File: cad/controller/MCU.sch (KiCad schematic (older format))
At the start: 19 parts

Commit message: Added decoupling inductors and capacitors
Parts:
- removed C?: C, symbol Device:C
- removed L?: L_Core_Ferrite, symbol Device:L_Core_Ferrite
- added C? (x2): 10uF, Capacitor_SMD:C_0603_1608Metric, symbol Device:C
- added C? (x3): 100nF, Capacitor_SMD:C_0603_1608Metric, symbol Device:C
- added FB?: BLM21, Inductor_SMD:L_0805_2012Metric, symbol Device:Ferrite_Bead
- added J?: Conn_01x04, symbol Connector_Generic:Conn_01x04
- added U?: TXB0104D, Package_SO:SOIC-14_3.9x8.7mm_P1.27mm, symbol Logic_LevelTranslator:TXB0104D
- C? (x3): value C -> 100nF; footprint (none) -> Capacitor_SMD:C_0603_1608Metric
- C? (x2): footprint (none) -> Capacitor_SMD:C_0603_1608Metric
- R? (x5): footprint (none) -> Resistor_SMD:R_0603_1608Metric
- Y?: value Crystal -> 18MHz
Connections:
- net labels added: CS, MISO, MOSI, SCLK
- net labels removed: ANA-
- wire segments 103 -> 132
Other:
- note added: "18 MHz\nECS-180-S-5PX-TR"
- note added: "TODO\n- Atmega328 pin mapping\n- Route ADC input 1"
- moved on the sheet: C?

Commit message: Ordered components
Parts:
- gave numbers to parts that had none: 25

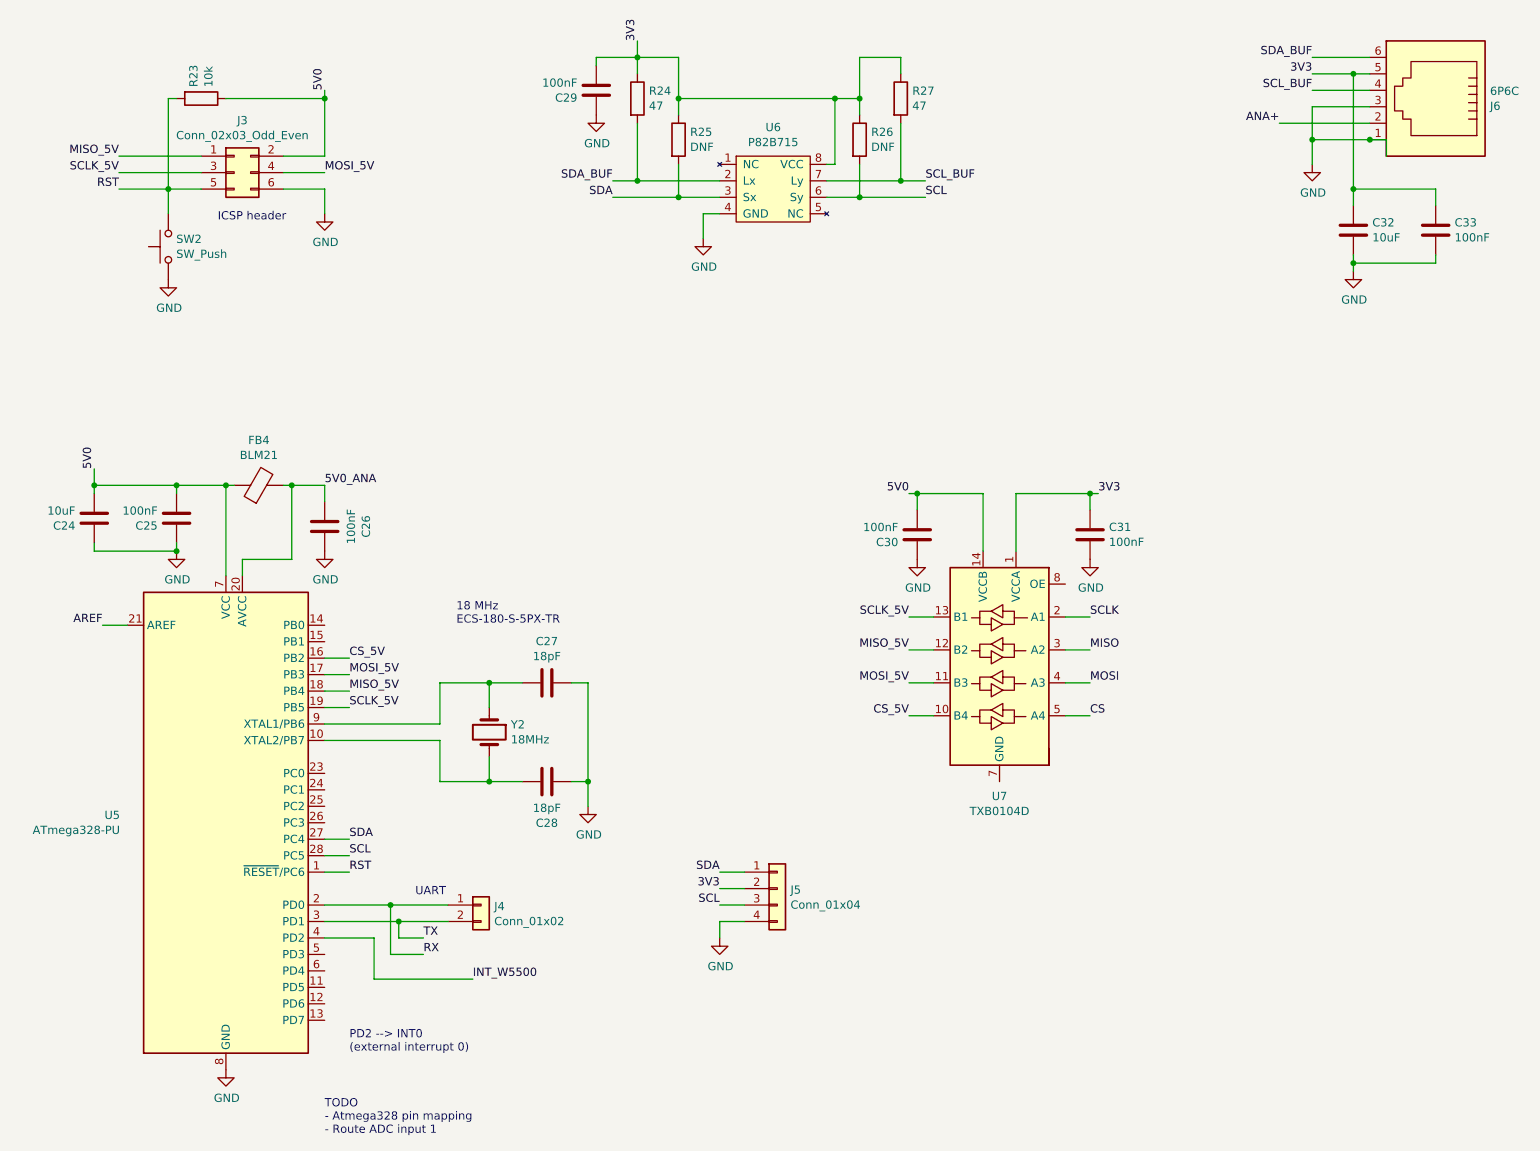
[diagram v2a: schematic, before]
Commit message: Changed I2C buffer to PCA1517, added termination network on RJ11 I2C lines
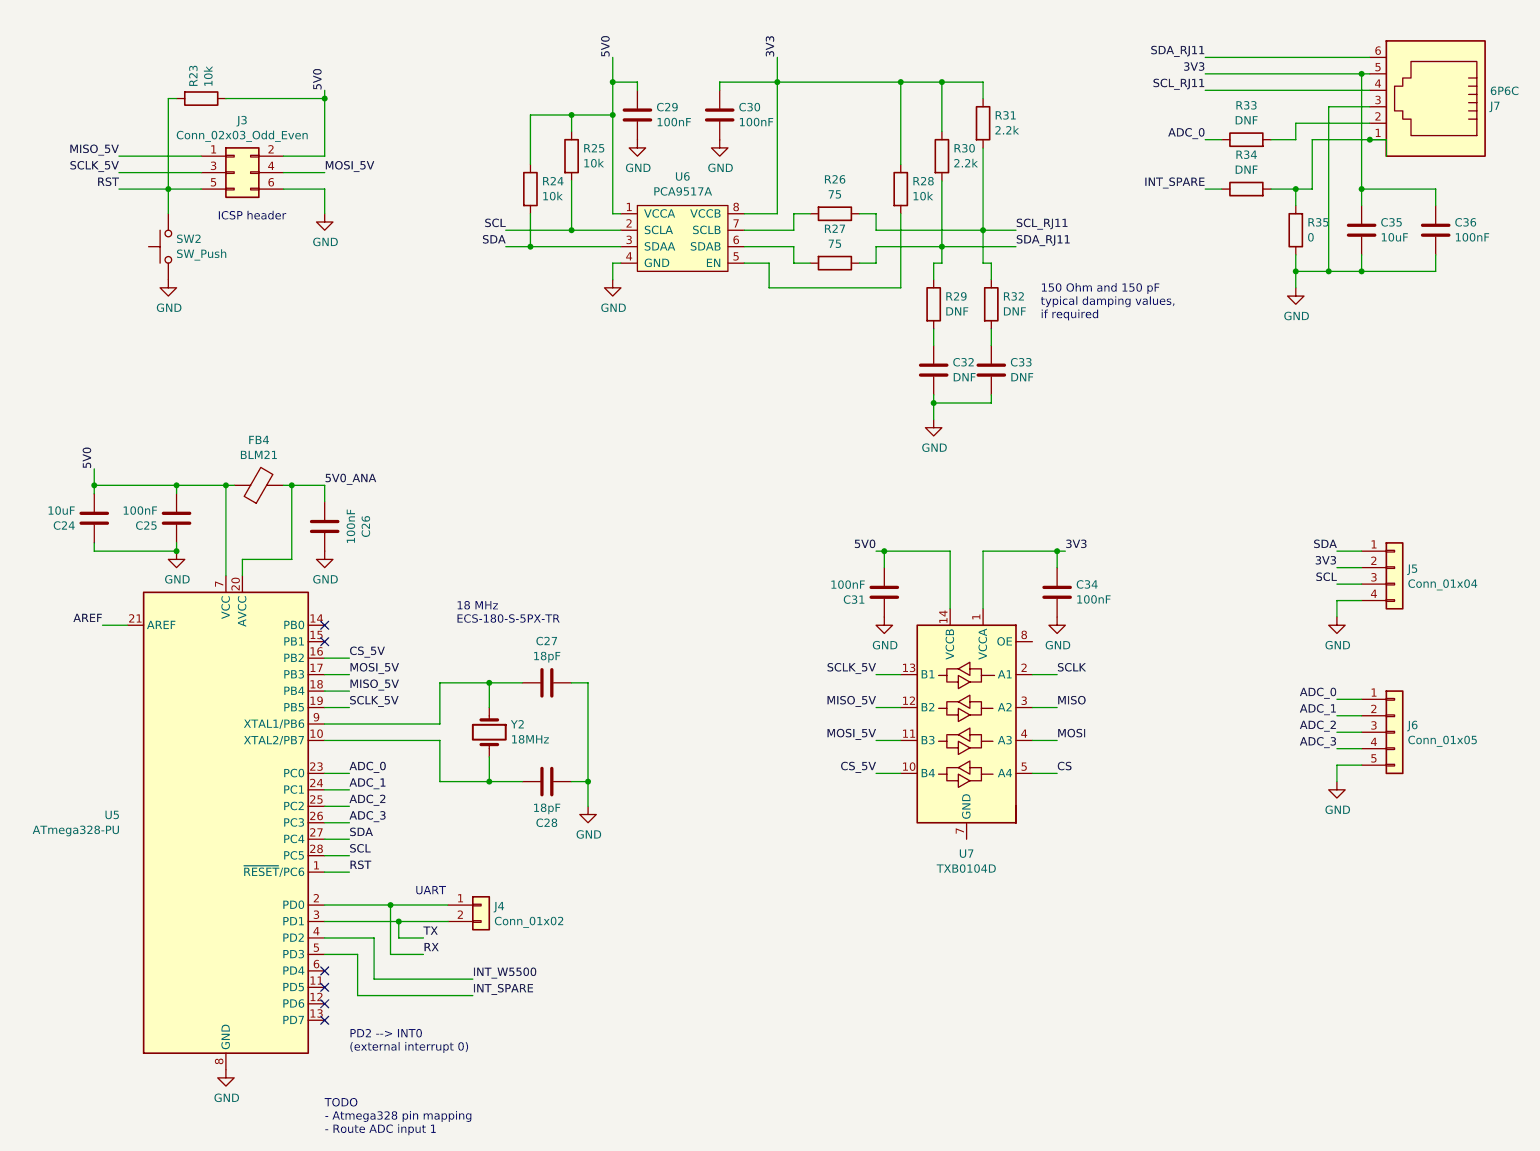
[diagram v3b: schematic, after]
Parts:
- removed U6: P82B715, symbol custom:P82B715
- added C30: 100nF, Capacitor_SMD:C_0603_1608Metric, symbol Device:C
- added C32, C33: DNF, Capacitor_SMD:C_0603_1608Metric, symbol Device:C
- added J6: Conn_01x05, symbol Connector_Generic:Conn_01x05
- added R28: 10k, Resistor_SMD:R_0603_1608Metric, symbol Device:R
- added R29, R32, R33, R34: DNF, Resistor_SMD:R_0603_1608Metric, symbol Device:R
- added R30, R31: 2.2k, Resistor_SMD:R_0603_1608Metric, symbol Device:R
- added R35: 0, Resistor_SMD:R_0603_1608Metric, symbol Device:R
- added U6: PCA9517A, symbol custom:PCA9517A
- R24: value 47 -> 10k
- R25: value DNF -> 10k
- R26: value DNF -> 75
- R27: value 47 -> 75
- renumbered C30 to C31, C31 to C34, C32 to C35, C33 to C36, J6 to J7
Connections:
- net 3V3: now also C30.1, R28.1, R30.1, R31.1, U6.8 (VCCB); no longer C29.2, R24.1, R25.1, R26.1, R27.1
- net 5V0: now also C29.1, R24.1, R25.1, U6.1 (VCCA)
- net GND: now also C29.2, C30.2, C32.2, C33.2, J6.5 (Pin_5), R35.1, U6.4 (GND); no longer C29.1, J7.1
- net SCL: now also R25.2, U6.2 (SCLA); no longer R26.2
- net SDA: now also R24.2, U6.3 (SDAA); no longer R25.2
- net ADC_0: now reaches U5.23 (PC0)
- net ADC_0: now also J6.1 (Pin_1), R33.1
- net ADC_1: now reaches U5.24 (PC1)
- net ADC_1: now also J6.2 (Pin_2)
- net ADC_2: now reaches U5.25 (PC2)
- net ADC_2: now also J6.3 (Pin_3)
- net ADC_3: now reaches U5.26 (PC3)
- net ADC_3: now also J6.4 (Pin_4)
- net INT_SPARE: now reaches U5.5 (PD3)
- net INT_SPARE: now also R34.1
- net ANA+: no longer names the net of J7.2
- net ANA+: now also R33.2
- net SCL_BUF: no longer names the net of R27.2
- net SCL_BUF: now also U6.6 (SDAB); no longer J7.4
- net SDA_BUF renamed SDA_RJ11
- net SDA_RJ11: now also R27.1, R29.1, R30.2; no longer R24.2
- new net: J7.1, R34.2, R35.2
- new net: R28.2, U6.5 (EN)
- new net: R26.2, U6.7 (SCLB)
- new net: C32.1, R29.2
- new net: C33.1, R32.2
- new net SCL_RJ11: J7.4, R26.1, R31.2, R32.1
- no-connect marks 0 -> 6
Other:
- note added: "150 Ohm and 150 pF\ntypical damping values,\nif required"
- moved on the sheet: C31, C34, C35, J5, U7

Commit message: Added custom libraries submodule and updated the symbol tables in the kicad projects
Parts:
- U6: symbol custom:PCA9517A -> custom_digital:PCA9517A
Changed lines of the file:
@@
 INT_SPARE
 $Comp
-L custom:PCA9517A U6
+L custom_digital:PCA9517A U6
 U 1 1 624DB520
 P 4950 1700

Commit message: Started associating footprints with controller schematic
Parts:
- J3: footprint (none) -> Connector_PinHeader_2.54mm:PinHeader_2x03_P2.54mm_Vertical
- J4: footprint (none) -> Connector_PinSocket_2.54mm:PinSocket_1x02_P2.54mm_Vertical
- J5: footprint (none) -> Connector_Molex:Molex_KK-254_AE-6410-04A_1x04_P2.54mm_Vertical
- J6: footprint (none) -> Connector_PinHeader_2.54mm:PinHeader_1x05_P2.54mm_Vertical
- SW2: footprint (none) -> Button_Switch_THT:SW_PUSH_6mm
- U6: footprint (none) -> Package_SO:TSSOP-8_3x3mm_P0.65mm
- Y2: footprint (none) -> Crystal:Crystal_SMD_HC49-SD_HandSoldering
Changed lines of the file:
@@
 F 0 "Y2" V 3704 5131 50  0000 L CNN
 F 1 "18MHz" V 3795 5131 50  0000 L CNN
-F 2 "" H 3750 5000 50  0001 C CNN
+F 2 "Crystal:Crystal_SMD_HC49-SD_HandSoldering" H 3750 5000 50  0001 C CNN
 F 3 "~" H 3750 5000 50  0001 C CNN
 	1    3750 5000
@@
 F 0 "J3" H 2250 1917 50  0000 C CNN
 F 1 "Conn_02x03_Odd_Even" H 2250 1826 50  0000 C CNN
-F 2 "" H 2200 1600 50  0001 C CNN
+F 2 "Connector_PinHeader_2.54mm:PinHeader_2x03_P2.54mm_Vertical" H 2200 1600 50  0001 C CNN
 F 3 "~" H 2200 1600 50  0001 C CNN
 	1    2200 1600
@@
 F 0 "SW2" V 1846 2002 50  0000 R CNN
 F 1 "SW_Push" V 1755 2002 50  0000 R CNN
-F 2 "" H 1800 2250 50  0001 C CNN
+F 2 "Button_Switch_THT:SW_PUSH_6mm" H 1800 2250 50  0001 C CNN
 F 3 "~" H 1800 2250 50  0001 C CNN
 	1    1800 2050
@@
 F 0 "J4" H 3780 6042 50  0000 L CNN
 F 1 "Conn_01x02" H 3780 5951 50  0000 L CNN
-F 2 "" H 3700 6050 50  0001 C CNN
+F 2 "Connector_PinSocket_2.54mm:PinSocket_1x02_P2.54mm_Vertical" H 3700 6050 50  0001 C CNN
 F 3 "~" H 3700 6050 50  0001 C CNN
 	1    3700 6050
@@
 F 0 "J5" H 9330 3992 50  0000 L CNN
 F 1 "Conn_01x04" H 9330 3901 50  0000 L CNN
-F 2 "" H 9250 4000 50  0001 C CNN
+F 2 "Connector_Molex:Molex_KK-254_AE-6410-04A_1x04_P2.54mm_Vertical" H 9250 4000 50  0001 C CNN
 F 3 "~" H 9250 4000 50  0001 C CNN
 	1    9250 4000
@@
 F 0 "J6" H 9330 5042 50  0000 L CNN
 F 1 "Conn_01x05" H 9330 4951 50  0000 L CNN
-F 2 "" H 9250 5000 50  0001 C CNN
+F 2 "Connector_PinHeader_2.54mm:PinHeader_1x05_P2.54mm_Vertical" H 9250 5000 50  0001 C CNN
 F 3 "~" H 9250 5000 50  0001 C CNN
 	1    9250 5000
@@
 F 0 "U6" H 4925 1775 50  0000 C CNN
 F 1 "PCA9517A" H 4925 1684 50  0000 C CNN
-F 2 "" H 4950 1700 50  0001 C CNN
+F 2 "Package_SO:TSSOP-8_3x3mm_P0.65mm" H 4950 1700 50  0001 C CNN
 F 3 "" H 4950 1700 50  0001 C CNN
 	1    4950 1700

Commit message: Ready to begin layout
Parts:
- J7: footprint (none) -> custom:E5566-Q0LK22-L
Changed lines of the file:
@@
 F 0 "J7" H 9170 1204 50  0000 R CNN
 F 1 "6P6C" H 9170 1295 50  0000 R CNN
-F 2 "" V 9500 1225 50  0001 C CNN
+F 2 "custom:E5566-Q0LK22-L" V 9500 1225 50  0001 C CNN
 F 3 "~" V 9500 1225 50  0001 C CNN
 	1    9500 1200

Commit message: controller placement in progress
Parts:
- Y2: footprint Crystal:Crystal_SMD_HC49-SD_HandSoldering -> Crystal:Crystal_SMD_HC49-SD
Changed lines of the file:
@@
 F 0 "Y2" V 3704 5131 50  0000 L CNN
 F 1 "18MHz" V 3795 5131 50  0000 L CNN
-F 2 "Crystal:Crystal_SMD_HC49-SD_HandSoldering" H 3750 5000 50  0001 C CNN
+F 2 "Crystal:Crystal_SMD_HC49-SD" H 3750 5000 50  0001 C CNN
 F 3 "~" H 3750 5000 50  0001 C CNN
 	1    3750 5000

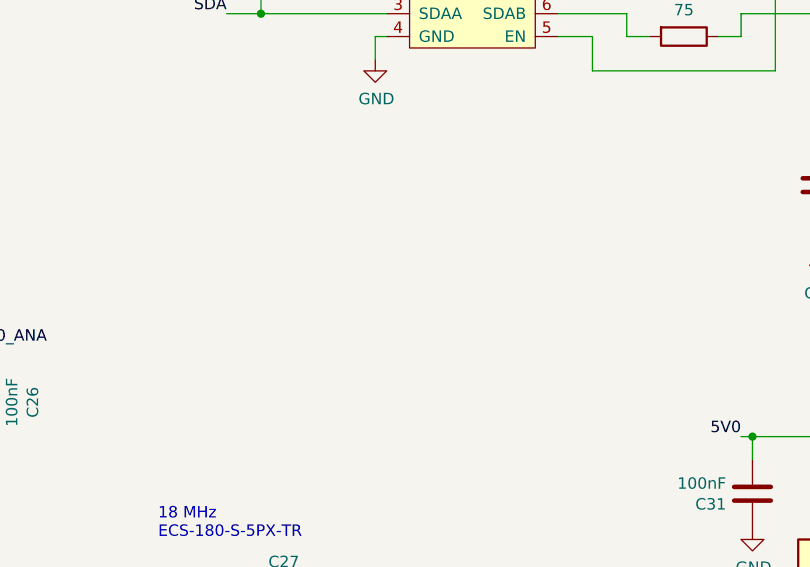
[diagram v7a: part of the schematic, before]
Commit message: Continued controller board placement
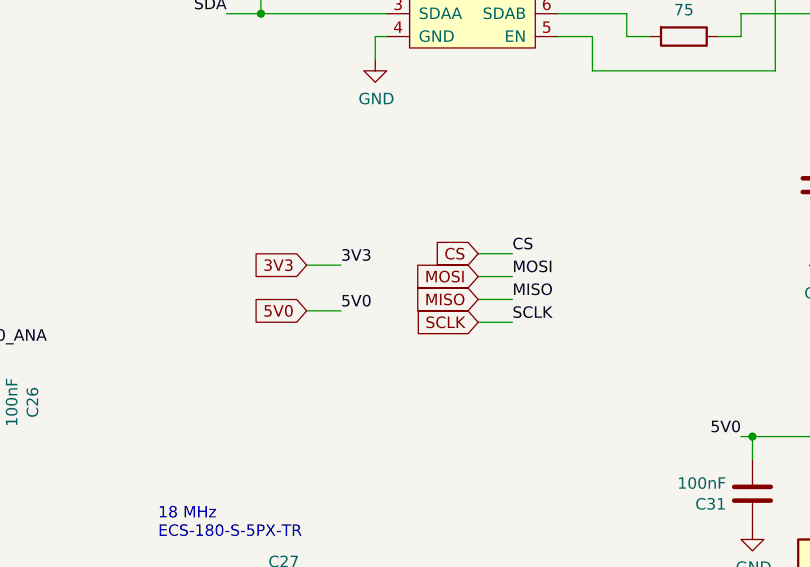
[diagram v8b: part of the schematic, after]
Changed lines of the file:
@@
 Text Notes 7100 2500 0    50   ~ 0
 150 Ohm and 150 pF\ntypical damping values,\nif required
+Text GLabel 4200 3150 0    50   Input ~ 0
+3V3
+Text Label 4350 3150 0    50   ~ 0
+3V3
+Wire Wire Line
+	4200 3150 4350 3150
+Text GLabel 4200 3350 0    50   Input ~ 0
+5V0
+Text Label 4350 3350 0    50   ~ 0
+5V0
+Wire Wire Line
+	4200 3350 4350 3350
+Text Label 5100 3400 0    50   ~ 0
+SCLK
+Text Label 5100 3300 0    50   ~ 0
+MISO
+Text Label 5100 3200 0    50   ~ 0
+MOSI
+Text Label 5100 3100 0    50   ~ 0
+CS
+Text GLabel 4950 3100 0    50   Input ~ 0
+CS
+Text GLabel 4950 3200 0    50   Input ~ 0
+MOSI
+Text GLabel 4950 3300 0    50   Input ~ 0
+MISO
+Text GLabel 4950 3400 0    50   Input ~ 0
+SCLK
+Wire Wire Line
+	4950 3100 5100 3100
+Wire Wire Line
+	4950 3200 5100 3200
+Wire Wire Line
+	4950 3300 5100 3300
+Wire Wire Line
+	4950 3400 5100 3400
 $EndSCHEMATC
